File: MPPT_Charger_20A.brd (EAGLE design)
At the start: 86 x 73.2 mm, 128 parts, among them IC2 LM4040CYM3-2.5, Q1 CSD18540Q5B, Q2 CSD18540Q5B, Q3 CSD18540Q5B, Q4 CSD18540Q5B, T1 MMBT3904, T2 MMBT3904, U1 LM5107, U2 LM2665, U3 MCP16331-CH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

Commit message: Minor changes + nice image from Aisler.net
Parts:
- C27, C28: value 12.5p -> 4.3p
- C7, C8: value 680µ -> 820µ
- Y2: value ABS25-32.768KHZ-T -> ABS25-32.768KHZ-6-T

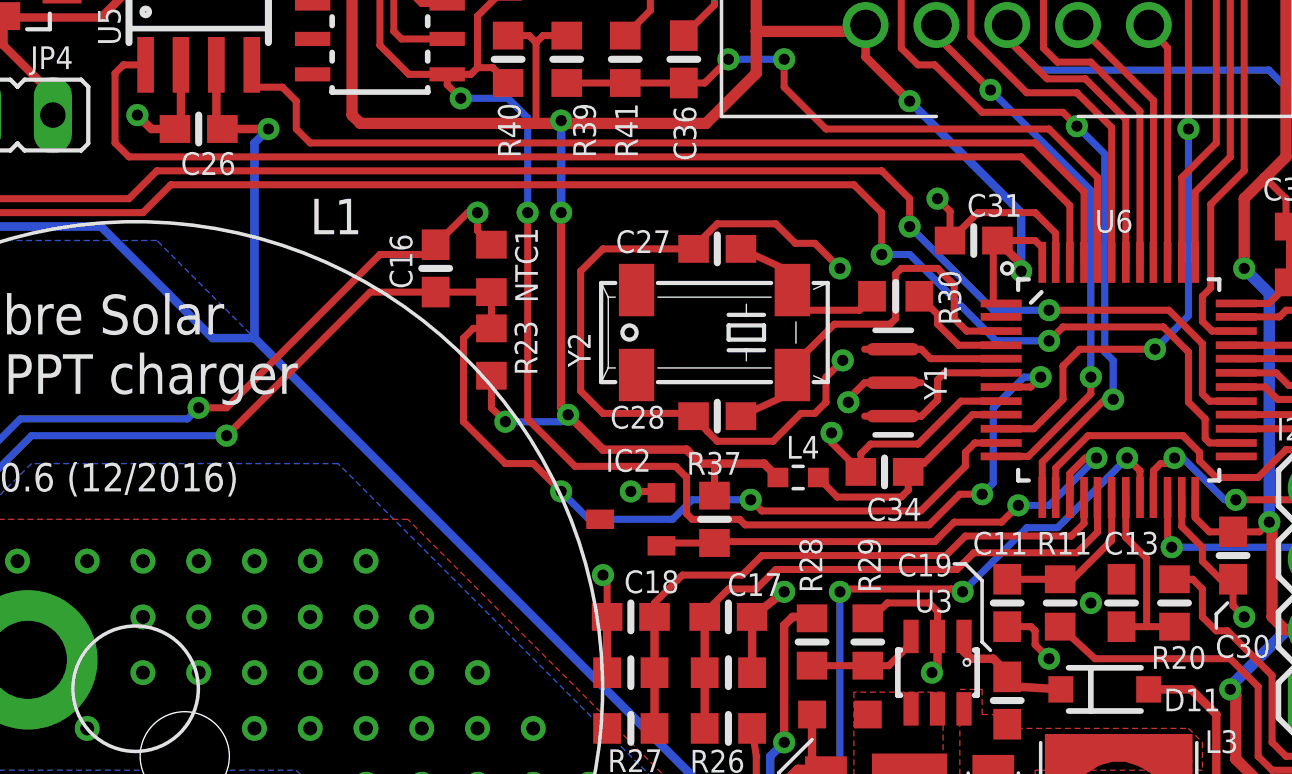
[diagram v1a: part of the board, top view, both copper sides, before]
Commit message: Fixing issues #12 and #11
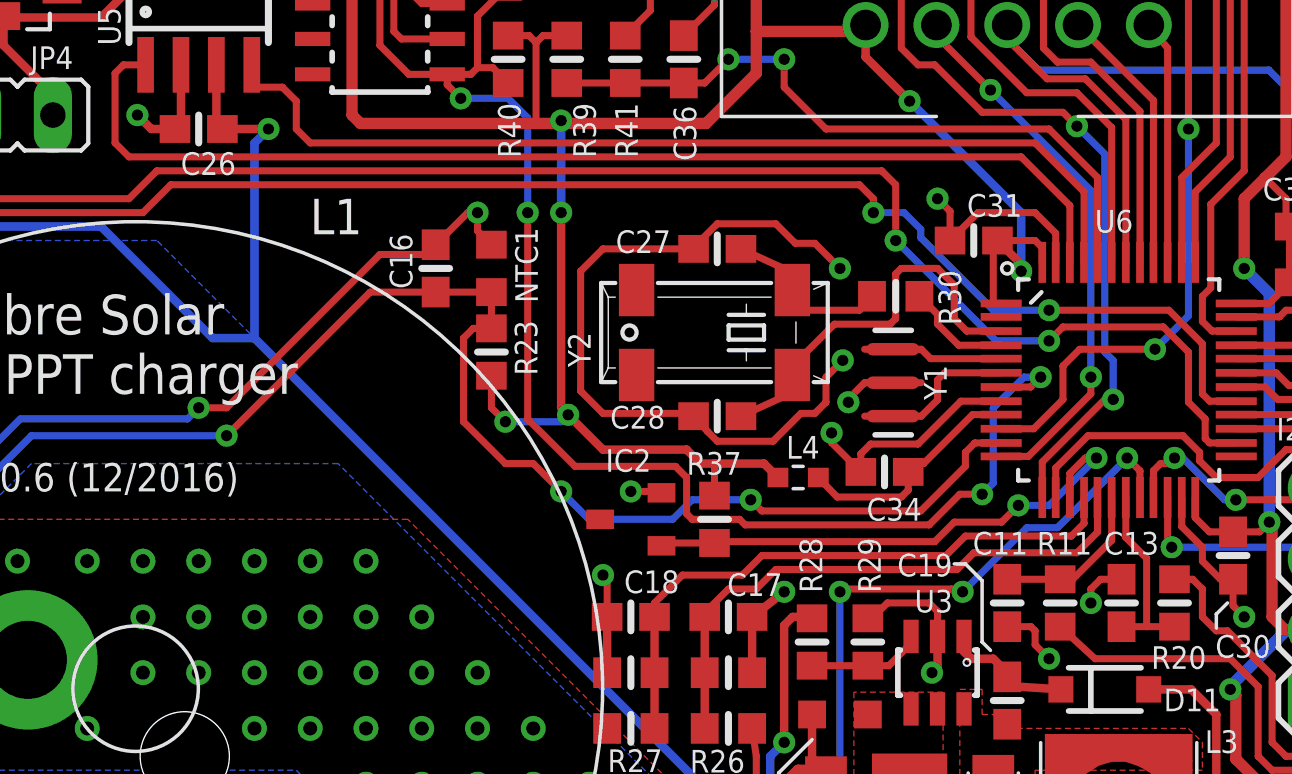
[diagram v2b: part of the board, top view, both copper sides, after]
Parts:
- R23: device rcl:R0603 -> LibreSolar:R0603
- R30: value 10k -> 0
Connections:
- net TIM1_CH1: now also U1.2; no longer U1.3
- net TIM1_CH1N: now also U1.3; no longer U1.2
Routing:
- net TIM1_CH1N: track 72.2 -> 74.3 mm
- net TIM1_CH1: track 72.3 -> 70.3 mm
- net GND: track 278.0 -> 279.7 mm
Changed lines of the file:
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@@
 <attribute name="VALUE" x="61.735" y="53.105" size="1.27" layer="27" rot="R180"/>
 </element>
-<element name="R30" library="LibreSolar" package="R0603" value="10k" x="67.5" y="55.5" smashed="yes" rot="R180">
+<element name="R30" library="LibreSolar" package="R0603" value="0" x="67.5" y="55.5" smashed="yes" rot="R180">
 <attribute name="OC_FARNELL" value="unknown" x="67.5" y="55.5" size="1.778" layer="27" rot="R180" display="off"/>
 <attribute name="MF" value="" x="67.5" y="55.5" size="1.778" layer="27" rot="R180" display="off"/>
@@
 <attribute name="VALUE" x="44.135" y="73.405" size="1.27" layer="27" rot="R180"/>
 </element>
-<element name="R23" library="rcl" package="R0603" value="10k" x="53" y="53.5" smashed="yes" rot="R270">
+<element name="R23" library="LibreSolar" package="R0603" value="10k" x="53" y="53.5" smashed="yes" rot="R270">
 <attribute name="MPN" value="" x="58" y="53.5" size="1.778" layer="27" rot="R270" display="off"/>
 <attribute name="OC_FARNELL" value="unknown" x="58" y="53.5" size="1.778" layer="27" rot="R270" display="off"/>
@@
 <via x="28" y="34" extent="1-16" drill="0.5"/>
 <via x="38" y="34" extent="1-16" drill="0.5"/>
-<wire x1="74.5" y1="44.5" x2="75.6" y2="45.35" width="0" layer="19" extent="1-1"/>
-<wire x1="82" y1="35.85" x2="82" y2="37" width="0" layer="19" extent="1-1"/>
+<wire x1="75.6" y1="45.35" x2="74.85" y2="45.35" width="0.254" layer="1"/>
+<wire x1="74.85" y1="45.35" x2="74.5" y2="45" width="0.254" layer="1"/>
+<wire x1="74.5" y1="45" x2="74.5" y2="44.5" width="0.254" layer="1"/>
+<wire x1="82" y1="37" x2="82" y2="35.85" width="0" layer="19" extent="1-1"/>
 </signal>
 <signal name="SW_NODE">
@@
 <signal name="TIM1_CH1">
 <contactref element="U6" pad="29"/>
-<contactref element="U1" pad="3"/>
 <wire x1="79.7164" y1="51.738" x2="78.762" y2="51.738" width="0.254" layer="1"/>
 <wire x1="78.762" y1="51.738" x2="78.5" y2="52" width="0.254" layer="1"/>
@@
 <via x="73" y="55" extent="1-16" drill="0.4"/>
 <wire x1="73" y1="55" x2="71" y2="55" width="0.254" layer="16"/>
-<wire x1="71" y1="55" x2="68" y2="58" width="0.254" layer="16"/>
-<via x="68" y="58" extent="1-16" drill="0.4"/>
-<wire x1="68" y1="58" x2="68" y2="59" width="0.254" layer="1"/>
-<wire x1="68" y1="59" x2="67" y2="60" width="0.254" layer="1"/>
-<wire x1="67" y1="60" x2="41" y2="60" width="0.254" layer="1"/>
-<wire x1="41" y1="60" x2="40" y2="59" width="0.254" layer="1"/>
-<wire x1="40" y1="59" x2="15.5" y2="59" width="0.254" layer="1"/>
-<wire x1="15.5" y1="59" x2="14.865" y2="58.365" width="0.254" layer="1"/>
-<wire x1="14.865" y1="58.365" x2="14.865" y2="56.7" width="0.254" layer="1"/>
+<contactref element="U1" pad="2"/>
+<wire x1="66.2" y1="59.5" x2="41.5" y2="59.5" width="0.254" layer="1"/>
+<wire x1="41.5" y1="59.5" x2="40.5" y2="58.5" width="0.254" layer="1"/>
+<wire x1="40.5" y1="58.5" x2="16.5" y2="58.5" width="0.254" layer="1"/>
+<wire x1="16.5" y1="58.5" x2="16.135" y2="58.135" width="0.254" layer="1"/>
+<wire x1="16.135" y1="58.135" x2="16.135" y2="56.7" width="0.254" layer="1"/>
+<wire x1="71" y1="55" x2="68.4" y2="57.6" width="0.254" layer="16"/>
+<wire x1="68.4" y1="57.6" x2="68.4" y2="57.9" width="0.254" layer="16"/>
+<wire x1="68.4" y1="57.9" x2="67.8" y2="58.5" width="0.254" layer="16"/>
+<wire x1="67.8" y1="58.5" x2="66.7" y2="58.5" width="0.254" layer="16"/>
+<via x="66.7" y="58.5" extent="1-16" drill="0.4"/>
+<wire x1="66.7" y1="58.5" x2="66.7" y2="59" width="0.254" layer="1"/>
+<wire x1="66.7" y1="59" x2="66.2" y2="59.5" width="0.254" layer="1"/>
 </signal>
 <signal name="USB_DM">
@@
 <signal name="TIM1_CH1N">
 <contactref element="U6" pad="26"/>
-<contactref element="U1" pad="2"/>
 <wire x1="79.7164" y1="50.2394" x2="78.7606" y2="50.2394" width="0.254" layer="1"/>
 <wire x1="78.7606" y1="50.2394" x2="78.6" y2="50.4" width="0.254" layer="1"/>
@@
 <via x="73" y="53.9" extent="1-16" drill="0.4"/>
 <wire x1="73" y1="53.9" x2="71.1" y2="53.9" width="0.254" layer="16"/>
-<wire x1="71.1" y1="53.9" x2="68" y2="57" width="0.254" layer="16"/>
-<wire x1="68" y1="57" x2="67" y2="57" width="0.254" layer="16"/>
-<via x="67" y="57" extent="1-16" drill="0.4"/>
-<wire x1="67" y1="57" x2="67" y2="58.5" width="0.254" layer="1"/>
-<wire x1="67" y1="58.5" x2="66" y2="59.5" width="0.254" layer="1"/>
-<wire x1="66" y1="59.5" x2="41.5" y2="59.5" width="0.254" layer="1"/>
-<wire x1="41.5" y1="59.5" x2="40.5" y2="58.5" width="0.254" layer="1"/>
-<wire x1="40.5" y1="58.5" x2="16.5" y2="58.5" width="0.254" layer="1"/>
-<wire x1="16.5" y1="58.5" x2="16.135" y2="58.135" width="0.254" layer="1"/>
-<wire x1="16.135" y1="58.135" x2="16.135" y2="56.7" width="0.254" layer="1"/>
+<wire x1="71.1" y1="53.9" x2="67.5" y2="57.5" width="0.254" layer="16"/>
+<contactref element="U1" pad="3"/>
+<wire x1="67" y1="60" x2="41" y2="60" width="0.254" layer="1"/>
+<wire x1="41" y1="60" x2="40" y2="59" width="0.254" layer="1"/>
+<wire x1="40" y1="59" x2="15.5" y2="59" width="0.254" layer="1"/>
+<wire x1="15.5" y1="59" x2="14.865" y2="58.365" width="0.254" layer="1"/>
+<wire x1="14.865" y1="58.365" x2="14.865" y2="56.7" width="0.254" layer="1"/>
+<via x="67.5" y="57.5" extent="1-16" drill="0.4"/>
+<wire x1="67.5" y1="57.5" x2="67.5" y2="59.5" width="0.254" layer="1"/>
+<wire x1="67.5" y1="59.5" x2="67" y2="60" width="0.254" layer="1"/>
 </signal>
 <signal name="I_LOAD">
